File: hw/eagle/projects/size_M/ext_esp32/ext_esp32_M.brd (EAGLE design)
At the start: 17 parts, among them IC1 CP2102

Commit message: completed pcb design for M.0 - made PCB order
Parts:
- added R5, R6: 12k, rcl:R0603
- C6: value 100n -> 2u2
- moved T2 0.33 mm to (11.3, 14.3)
- moved R4 0.31 mm to (13.5, 16.9)
- moved R3 0.13 mm to (7.57, 15.0)
- moved IC1 0.10 mm to (9.96, 8.97)
- moved JP1 0.10 mm to (19.6, 13.0)
- moved JP2 0.10 mm to (1.40, 13.0)
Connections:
- removed net N$12: C4.2, C5.2, IC1.7, IC1.8, JP1.1, USB.VUSB
- new net VUSB: C4.2, C5.2, IC1.7, IC1.8, JP1.2, USB.VUSB
- net GND: no longer JP1.2
- net N$10: now also R5.1
- net N$11: now also R6.2
- net VDD: now also R5.2, R6.1
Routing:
- net N$12: track 25.1 -> 0.00 mm, vias 2 -> 0
- net VUSB: track 0.00 -> 22.7 mm, vias 0 -> 2
- net VDD: track 48.4 -> 54.9 mm, vias 2 -> 5
- net GND: track 108.7 -> 111.2 mm
- net N$11: track 21.1 -> 23.4 mm
- net N$10: track 8.99 -> 9.96 mm
- net N$6: track 13.8 -> 13.1 mm

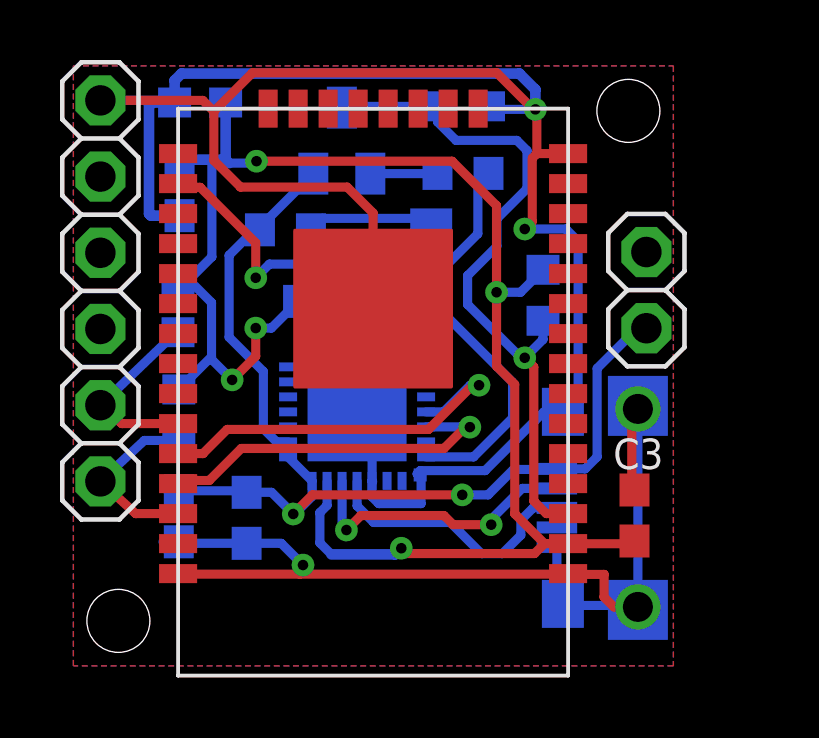
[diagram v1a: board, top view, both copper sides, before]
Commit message: fix for esp board (RST -> RTS)
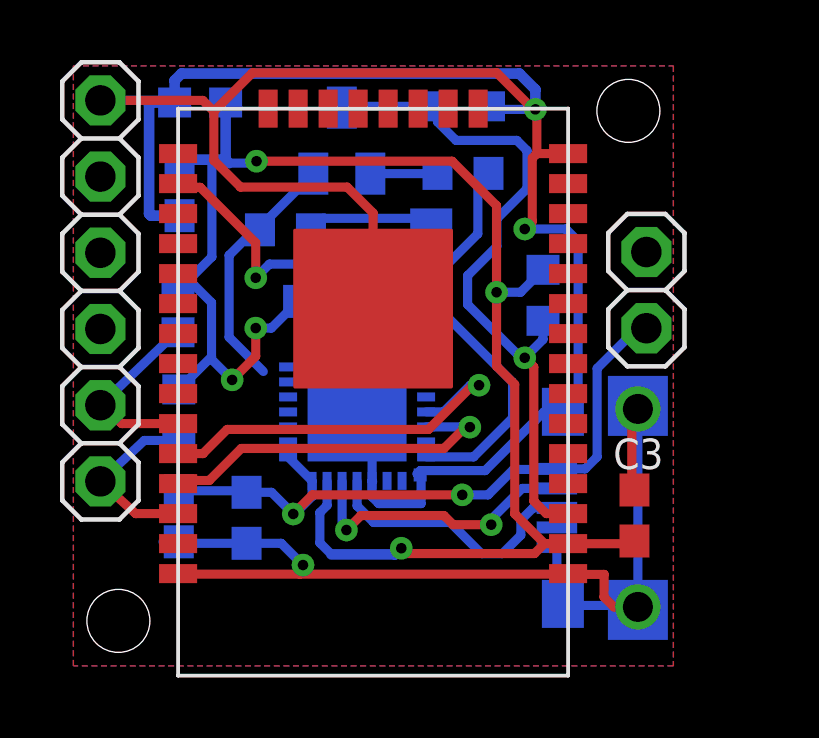
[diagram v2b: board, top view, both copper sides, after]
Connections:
- net N$9 renamed DTR
- removed net N$8: IC1.9, R3.1, T1.E
- new net RTS: IC1.24, R3.1, T1.E
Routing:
- net N$8: track 11.2 -> 0.00 mm
- net RTS: track 0.00 -> 8.34 mm
